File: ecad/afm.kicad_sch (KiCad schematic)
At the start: 0 parts

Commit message: things
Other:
- note removed: "- [x] check if the PDIC and Laser have different GNDS: YES; can i still connect them? - [x] schematic: unity-gain amps for FES buffers - [ ] figure out basic voicecoil driving. sch + proto - [ ] proto the LD apc. - [ ] characterize FES signals at focus levels (using voicecoils) - [ ] figure out if more signal conditioning is needed - [ ] research ADCs"
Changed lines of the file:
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@@
-		)
-	)
-	(text "- [x] check if the PDIC and Laser have different GNDS: YES; can i still connect them?\n\n- [x] schematic: unity-gain amps for FES buffers\n- [ ] figure out basic voicecoil driving. sch + proto\n\n- [ ] proto the LD apc.\n- [ ] characterize FES signals at focus levels (using voicecoils)\n\n- [ ] figure out if more signal conditioning is needed\n- [ ] research ADCs"
-		(exclude_from_sim no)
-		(at 13.716 25.4 0)
-		(effects
-			(font
-				(size 1.27 1.27)
-			)
-			(justify left)
 		)
 	)

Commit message: vca driver draft
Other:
- added sheet VCA Driver (vca_driver.kicad_sch)
- note removed: "Voicecoil Driver stuff"
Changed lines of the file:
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@@
-		)
-	)
-	(rectangle
-		(start 82.55 54.61)
-		(end 113.03 72.39)
-		(stroke
-			(width 0)
-			(type default)
-		)
-		(fill
-			(type none)
-		)
-	)
-	(text "Voicecoil Driver stuff"
-		(exclude_from_sim no)
-		(at 97.028 63.5 0)
-		(effects
-			(font
-				(size 1.27 1.27)
-			)
 		)
 	)
@@
 		(pts
 			(xy 67.31 92.71) (xy 90.17 92.71)
-		)
-		(stroke
-			(width 0)
-			(type default)
-		)
-	)
-	(polyline
-		(pts
-			(xy 113.03 64.77) (xy 147.32 64.77)
 		)
 		(stroke
@@
 		)
 	)
-	(polyline
-		(pts
-			(xy 147.32 74.93) (xy 147.32 83.82)
-		)
-		(stroke
-			(width 0)
-			(type default)
-		)
-	)
 	(wire
 		(pts
@@
 		(pts
 			(xy 40.64 106.68) (xy 49.53 106.68)
-		)
-		(stroke
-			(width 0)
-			(type default)
-		)
-	)
-	(polyline
-		(pts
-			(xy 147.32 64.77) (xy 147.32 74.93)
 		)
 		(stroke
@@
 		)
 	)
+	(sheet
+		(at 91.44 60.96)
+		(size 17.78 7.62)
+		(exclude_from_sim no)
+		(in_bom yes)
+		(on_board yes)
+		(dnp no)
+		(fields_autoplaced yes)
+		(stroke
+			(width 0.1524)
+			(type solid)
+		)
+		(fill
+			(color 0 0 0 0)
+		)
+		(property "Sheetname" "VCA Driver"
+			(at 91.44 60.2484 0)
+			(show_name no)
+			(do_not_autoplace no)
+			(effects
+				(font
+					(size 1.27 1.27)
+				)
+				(justify left bottom)
+			)
+		)
+		(property "Sheetfile" "vca_driver.kicad_sch"
+			(at 91.44 69.1646 0)
+			(hide yes)
+			(show_name no)
+			(do_not_autoplace no)
+			(effects
+				(font
+					(size 1.27 1.27)
+				)
+				(justify left top)
+			)
+		)
+		(instances
+			(project "afm"
+				(path "/62de9aa8-4539-4ecb-8acc-2c7a46b3005b"
+					(page "9")
+				)
+			)
+		)
+	)

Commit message: stuff
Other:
- sheet MCU ports: added VCA_Vref; removed none
- sheet VCA Driver ports: added DRV_CURR_Vref, VCA+, VCA-; removed none

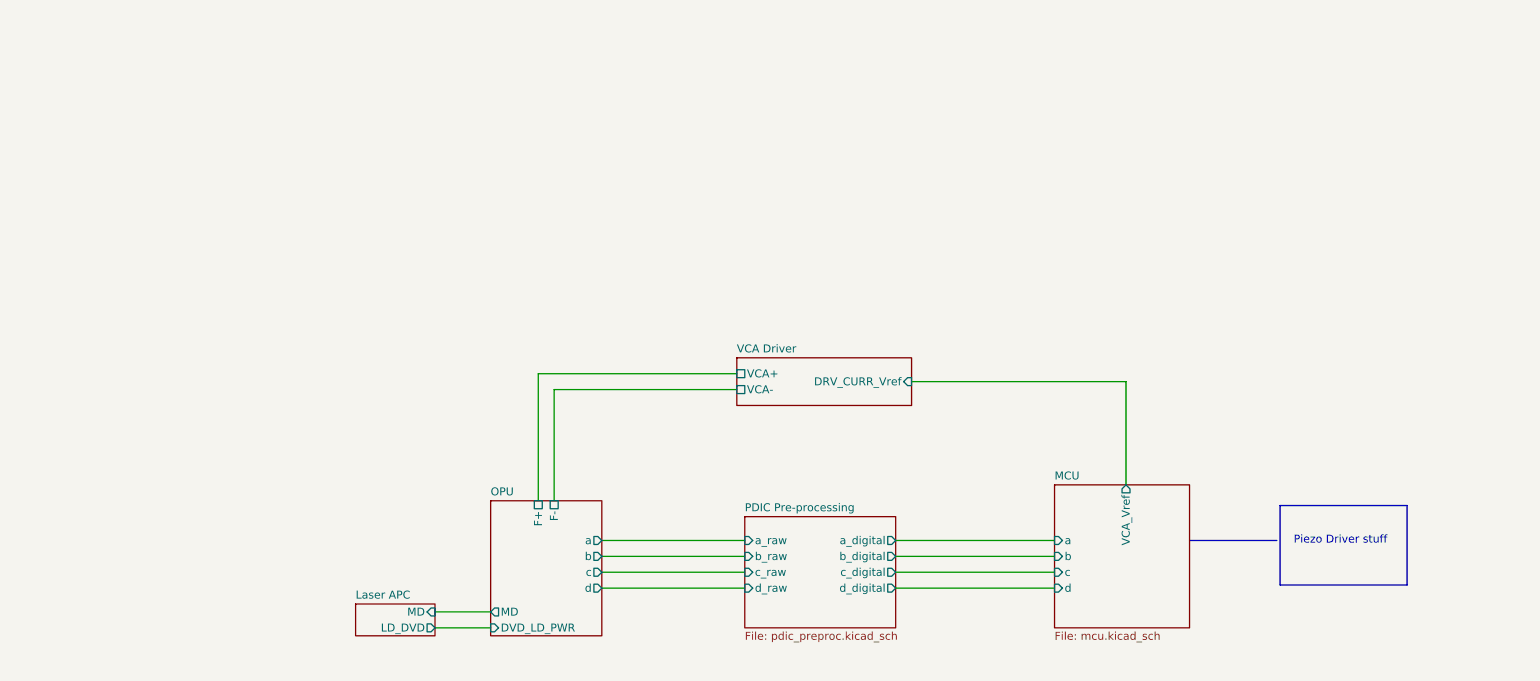
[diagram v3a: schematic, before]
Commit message: reorg; dac symbols
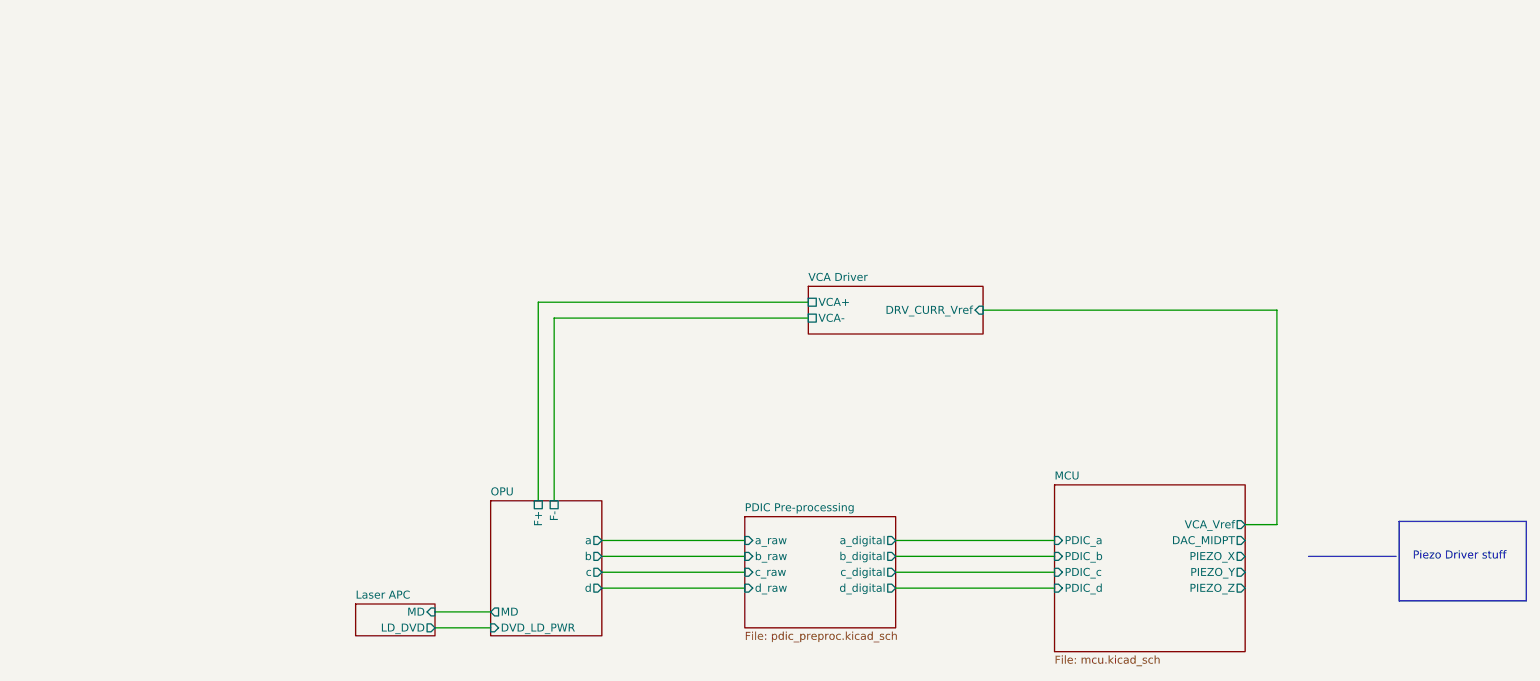
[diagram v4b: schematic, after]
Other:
- sheet MCU ports: added DAC_MIDPT, PDIC_a, PDIC_b, PDIC_c, PDIC_d, PIEZO_X, PIEZO_Y, PIEZO_Z; removed a, b, c, d
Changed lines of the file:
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@@
 	)
 	(rectangle
-		(start 216.408 93.472)
-		(end 236.728 106.172)
+		(start 235.458 96.012)
+		(end 255.778 108.712)
 		(stroke
 			(width 0)
@@
 	(text "Piezo Driver stuff"
 		(exclude_from_sim no)
-		(at 226.06 99.06 0)
+		(at 245.11 101.6 0)
 		(effects
 			(font
@@
 	(wire
 		(pts
-			(xy 157.48 73.66) (xy 191.77 73.66)
-		)
-		(stroke
-			(width 0)
-			(type default)
-		)
-	)
-	(wire
-		(pts
-			(xy 191.77 73.66) (xy 191.77 90.17)
+			(xy 168.91 62.23) (xy 215.9 62.23)
+		)
+		(stroke
+			(width 0)
+			(type default)
+		)
+	)
+	(wire
+		(pts
+			(xy 215.9 62.23) (xy 215.9 96.52)
 		)
 		(stroke
@@
 	(wire
 		(pts
-			(xy 100.33 74.93) (xy 129.54 74.93)
+			(xy 100.33 63.5) (xy 140.97 63.5)
 		)
 		(stroke
@@
 	(polyline
 		(pts
-			(xy 201.93 99.06) (xy 215.9 99.06)
+			(xy 220.98 101.6) (xy 234.95 101.6)
 		)
 		(stroke
@@
 	(wire
 		(pts
-			(xy 97.79 92.71) (xy 97.79 72.39)
+			(xy 97.79 92.71) (xy 97.79 60.96)
 		)
 		(stroke
@@
 	(wire
 		(pts
-			(xy 97.79 72.39) (xy 129.54 72.39)
+			(xy 97.79 60.96) (xy 140.97 60.96)
 		)
 		(stroke
@@
 	(wire
 		(pts
-			(xy 100.33 92.71) (xy 100.33 74.93)
+			(xy 100.33 92.71) (xy 100.33 63.5)
+		)
+		(stroke
+			(width 0)
+			(type default)
+		)
+	)
+	(wire
+		(pts
+			(xy 215.9 96.52) (xy 210.82 96.52)
 		)
 		(stroke
@@
 	)
 	(sheet
-		(at 129.54 69.85)
+		(at 140.97 58.42)
 		(size 27.94 7.62)
 		(exclude_from_sim no)
@@
 		)
 		(property "Sheetname" "VCA Driver"
-			(at 129.54 69.1384 0)
+			(at 140.97 57.7084 0)
 			(show_name no)
 			(do_not_autoplace no)
@@
 		)
 		(property "Sheetfile" "vca_driver.kicad_sch"
-			(at 129.54 78.0546 0)
+			(at 140.97 66.6246 0)
 			(hide yes)
 			(show_name no)
@@
 		)
 		(pin "VCA+" passive
-			(at 129.54 72.39 180)
+			(at 140.97 60.96 180)
 			(effects
 				(font
@@
 		)
 		(pin "VCA-" passive
-			(at 129.54 74.93 180)
+			(at 140.97 63.5 180)
 			(effects
 				(font
@@
 		)
 		(pin "DRV_CURR_Vref" input
-			(at 157.48 73.66 0)
+			(at 168.91 62.23 0)
 			(effects
 				(font
@@
 	(sheet
 		(at 180.34 90.17)
-		(size 21.59 22.86)
+		(size 30.48 26.67)
 		(exclude_from_sim no)
 		(in_bom yes)
@@
 		)
 		(property "Sheetfile" "mcu.kicad_sch"
-			(at 180.34 113.6146 0)
+			(at 180.34 117.4246 0)
 			(show_name no)
 			(do_not_autoplace no)
@@
 			)
 		)
-		(pin "a" input
+		(pin "VCA_Vref" output
+			(at 210.82 96.52 0)
+			(effects
+				(font
+					(size 1.27 1.27)
+				)
+				(justify right)
+			)
+		)
+		(pin "DAC_MIDPT" output
+			(at 210.82 99.06 0)
+			(effects
+				(font
+					(size 1.27 1.27)
+				)
+				(justify right)
+			)
+		)
+		(pin "PDIC_a" input
 			(at 180.34 99.06 180)
 			(effects
@@
 			)
 		)
-		(pin "b" input
+		(pin "PIEZO_X" output
+			(at 210.82 101.6 0)
+			(effects
+				(font
+					(size 1.27 1.27)
+				)
+				(justify right)
+			)
+		)
+		(pin "PIEZO_Z" output
+			(at 210.82 106.68 0)
+			(effects
+				(font
+					(size 1.27 1.27)
+				)
+				(justify right)
+			)
+		)
+		(pin "PIEZO_Y" output
+			(at 210.82 104.14 0)
+			(effects
+				(font
+					(size 1.27 1.27)
+				)
+				(justify right)
+			)
+		)
+		(pin "PDIC_c" input
+			(at 180.34 104.14 180)
+			(effects
+				(font
+					(size 1.27 1.27)
+				)
+				(justify left)
+			)
+		)
+		(pin "PDIC_b" input
 			(at 180.34 101.6 180)
 			(effects
@@
 			)
 		)
-		(pin "c" input
-			(at 180.34 104.14 180)
-			(effects
-				(font
-					(size 1.27 1.27)
-				)
-				(justify left)
-			)
-		)
-		(pin "d" input
+		(pin "PDIC_d" input
 			(at 180.34 106.68 180)
 			(effects
@@
 			)
 		)
-		(pin "VCA_Vref" output
-			(at 191.77 90.17 90)
-			(effects
-				(font
-					(size 1.27 1.27)
-				)
-				(justify right)
-			)
-		)

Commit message: vca drv ref
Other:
- sheet MCU ports: added DAC_MID_Vref, VCA_DRV; removed DAC_MIDPT, VCA_Vref
- sheet VCA Driver ports: added DAC_MIDPT; removed none
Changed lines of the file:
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@@
 	(wire
 		(pts
-			(xy 168.91 62.23) (xy 215.9 62.23)
-		)
-		(stroke
-			(width 0)
-			(type default)
-		)
-	)
-	(wire
-		(pts
-			(xy 215.9 62.23) (xy 215.9 96.52)
+			(xy 213.36 71.12) (xy 213.36 96.52)
 		)
 		(stroke
@@
 	(wire
 		(pts
-			(xy 100.33 63.5) (xy 140.97 63.5)
+			(xy 100.33 71.12) (xy 138.43 71.12)
+		)
+		(stroke
+			(width 0)
+			(type default)
+		)
+	)
+	(wire
+		(pts
+			(xy 166.37 71.12) (xy 213.36 71.12)
 		)
 		(stroke
@@
 	(wire
 		(pts
-			(xy 97.79 92.71) (xy 97.79 60.96)
+			(xy 215.9 99.06) (xy 215.9 68.58)
+		)
+		(stroke
+			(width 0)
+			(type default)
+		)
+	)
+	(wire
+		(pts
+			(xy 97.79 92.71) (xy 97.79 68.58)
 		)
 		(stroke
@@
 	(wire
 		(pts
-			(xy 97.79 60.96) (xy 140.97 60.96)
+			(xy 210.82 99.06) (xy 215.9 99.06)
+		)
+		(stroke
+			(width 0)
+			(type default)
+		)
+	)
+	(wire
+		(pts
+			(xy 97.79 68.58) (xy 138.43 68.58)
 		)
 		(stroke
@@
 	(wire
 		(pts
+			(xy 166.37 68.58) (xy 215.9 68.58)
+		)
+		(stroke
+			(width 0)
+			(type default)
+		)
+	)
+	(wire
+		(pts
 			(xy 107.95 106.68) (xy 130.81 106.68)
 		)
@@
 	(wire
 		(pts
-			(xy 100.33 92.71) (xy 100.33 63.5)
-		)
-		(stroke
-			(width 0)
-			(type default)
-		)
-	)
-	(wire
-		(pts
-			(xy 215.9 96.52) (xy 210.82 96.52)
+			(xy 100.33 92.71) (xy 100.33 71.12)
+		)
+		(stroke
+			(width 0)
+			(type default)
+		)
+	)
+	(wire
+		(pts
+			(xy 213.36 96.52) (xy 210.82 96.52)
 		)
 		(stroke
@@
 	)
 	(sheet
-		(at 140.97 58.42)
+		(at 138.43 66.04)
 		(size 27.94 7.62)
 		(exclude_from_sim no)
@@
 		)
 		(property "Sheetname" "VCA Driver"
-			(at 140.97 57.7084 0)
+			(at 138.43 65.3284 0)
 			(show_name no)
 			(do_not_autoplace no)
@@
 		)
 		(property "Sheetfile" "vca_driver.kicad_sch"
-			(at 140.97 66.6246 0)
+			(at 138.43 74.2446 0)
 			(hide yes)
 			(show_name no)
@@
 		)
 		(pin "VCA+" passive
-			(at 140.97 60.96 180)
+			(at 138.43 68.58 180)
 			(effects
 				(font
@@
 		)
 		(pin "VCA-" passive
-			(at 140.97 63.5 180)
+			(at 138.43 71.12 180)
 			(effects
 				(font
@@
 		)
 		(pin "DRV_CURR_Vref" input
-			(at 168.91 62.23 0)
+			(at 166.37 71.12 0)
+			(effects
+				(font
+					(size 1.27 1.27)
+				)
+				(justify right)
+			)
+		)
+		(pin "DAC_MIDPT" input
+			(at 166.37 68.58 0)
 			(effects
 				(font
@@
 			)
 		)
-		(pin "VCA_Vref" output
-			(at 210.82 96.52 0)
-			(effects
-				(font
-					(size 1.27 1.27)
-				)
-				(justify right)
-			)
-		)
-		(pin "DAC_MIDPT" output
-			(at 210.82 99.06 0)
-			(effects
-				(font
-					(size 1.27 1.27)
-				)
-				(justify right)
-			)
-		)
 		(pin "PDIC_a" input
 			(at 180.34 99.06 180)
@@
 			)
 		)
+		(pin "DAC_MID_Vref" output
+			(at 210.82 99.06 0)
+			(effects
+				(font
+					(size 1.27 1.27)
+				)
+				(justify right)
+			)
+		)
+		(pin "VCA_DRV" output
+			(at 210.82 96.52 0)
+			(effects
+				(font
+					(size 1.27 1.27)
+				)
+				(justify right)
+			)
+		)

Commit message: need to sweep
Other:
- sheet VCA Driver ports: added DAC_MIDPT_Vref, VCA_DRV; removed DAC_MIDPT, DRV_CURR_Vref
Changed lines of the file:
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@@
 			)
 		)
-		(pin "DRV_CURR_Vref" input
+		(pin "VCA_DRV" input
 			(at 166.37 71.12 0)
 			(effects
@@
 			)
 		)
-		(pin "DAC_MIDPT" input
+		(pin "DAC_MIDPT_Vref" input
 			(at 166.37 68.58 0)
 			(effects
